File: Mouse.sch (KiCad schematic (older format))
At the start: 27 parts, among them J1 Conn_01x05_Male, U1 Left click, U2 Middle click, U3 Right Click, U4 LQ1, U5 Optical_Sensor

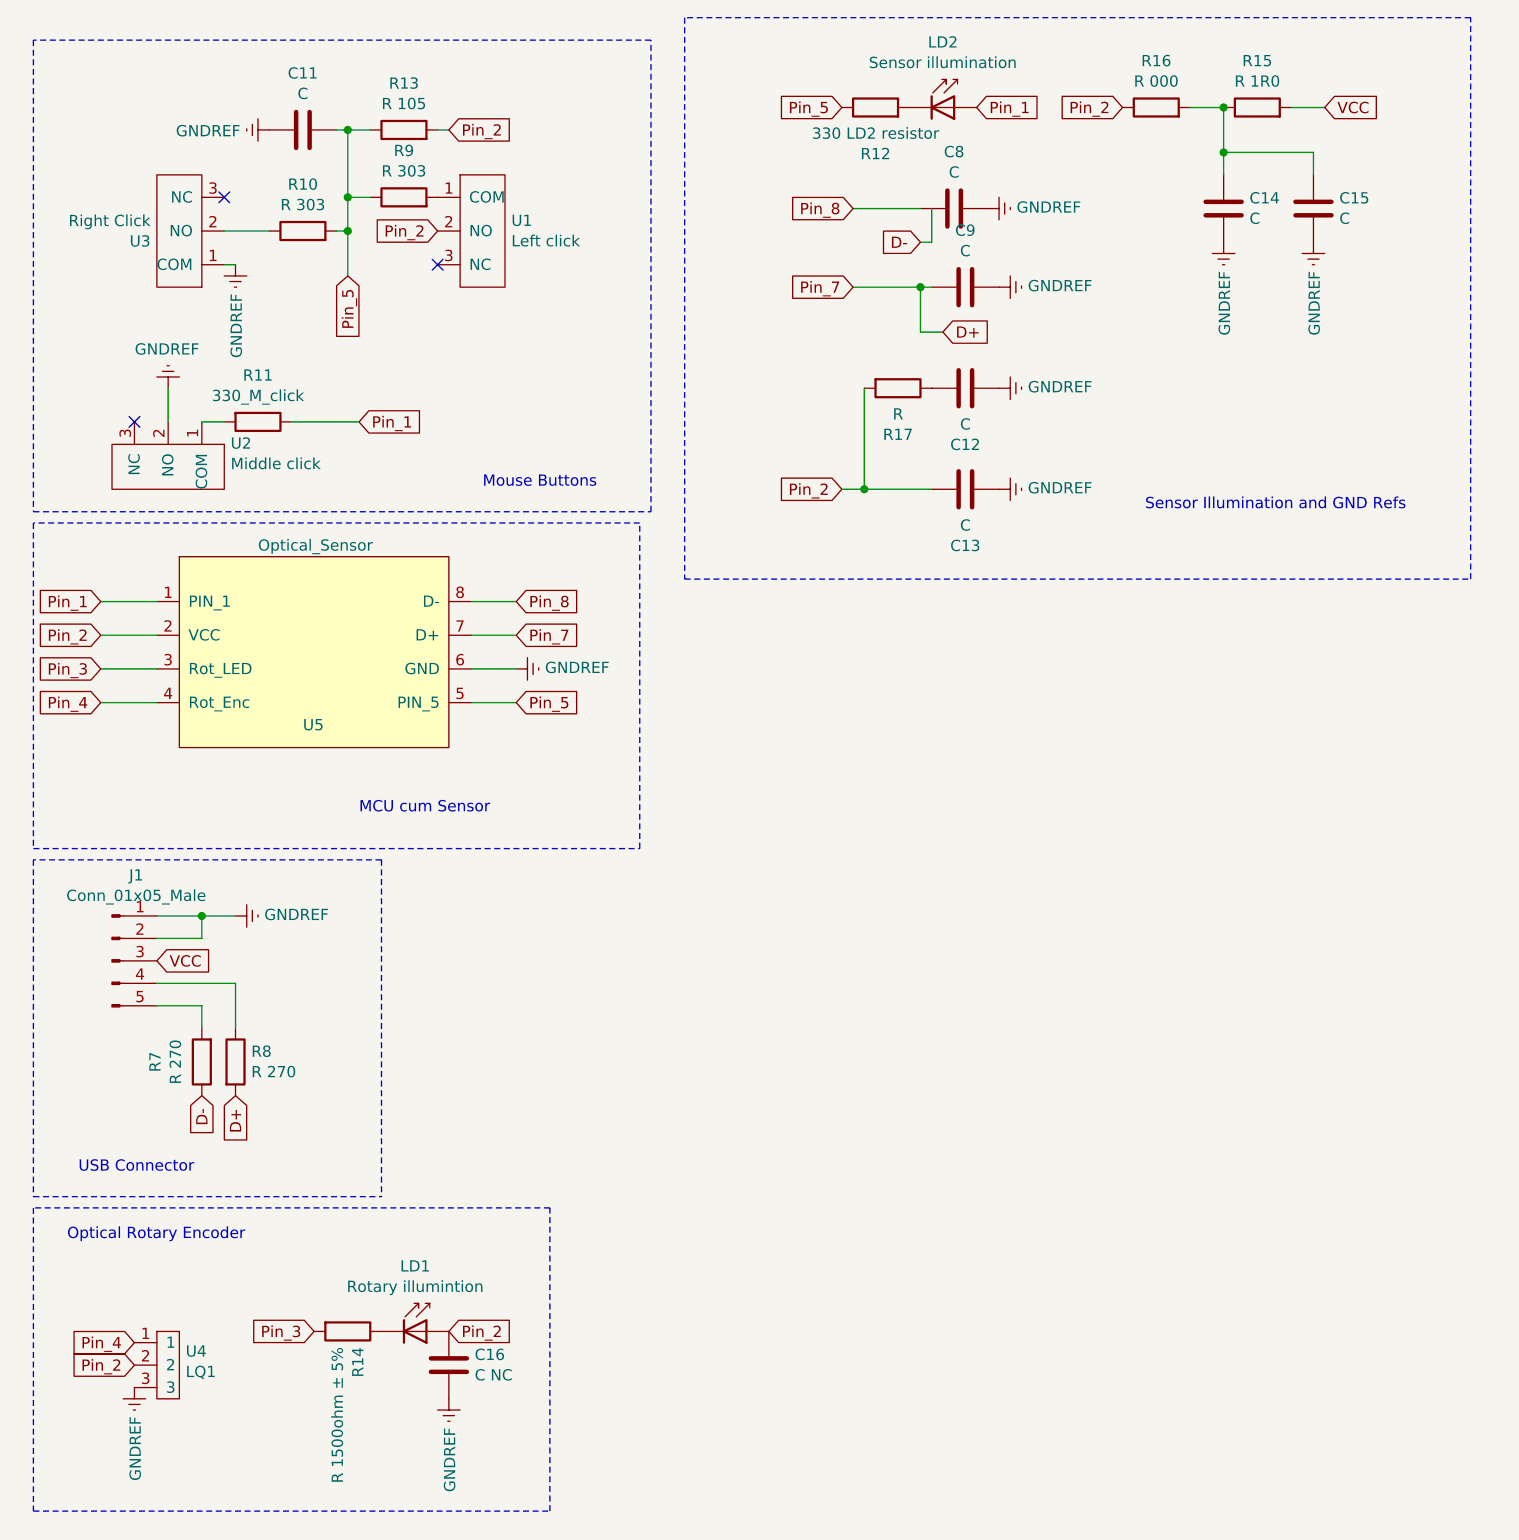
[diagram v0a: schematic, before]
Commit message: Updated layout
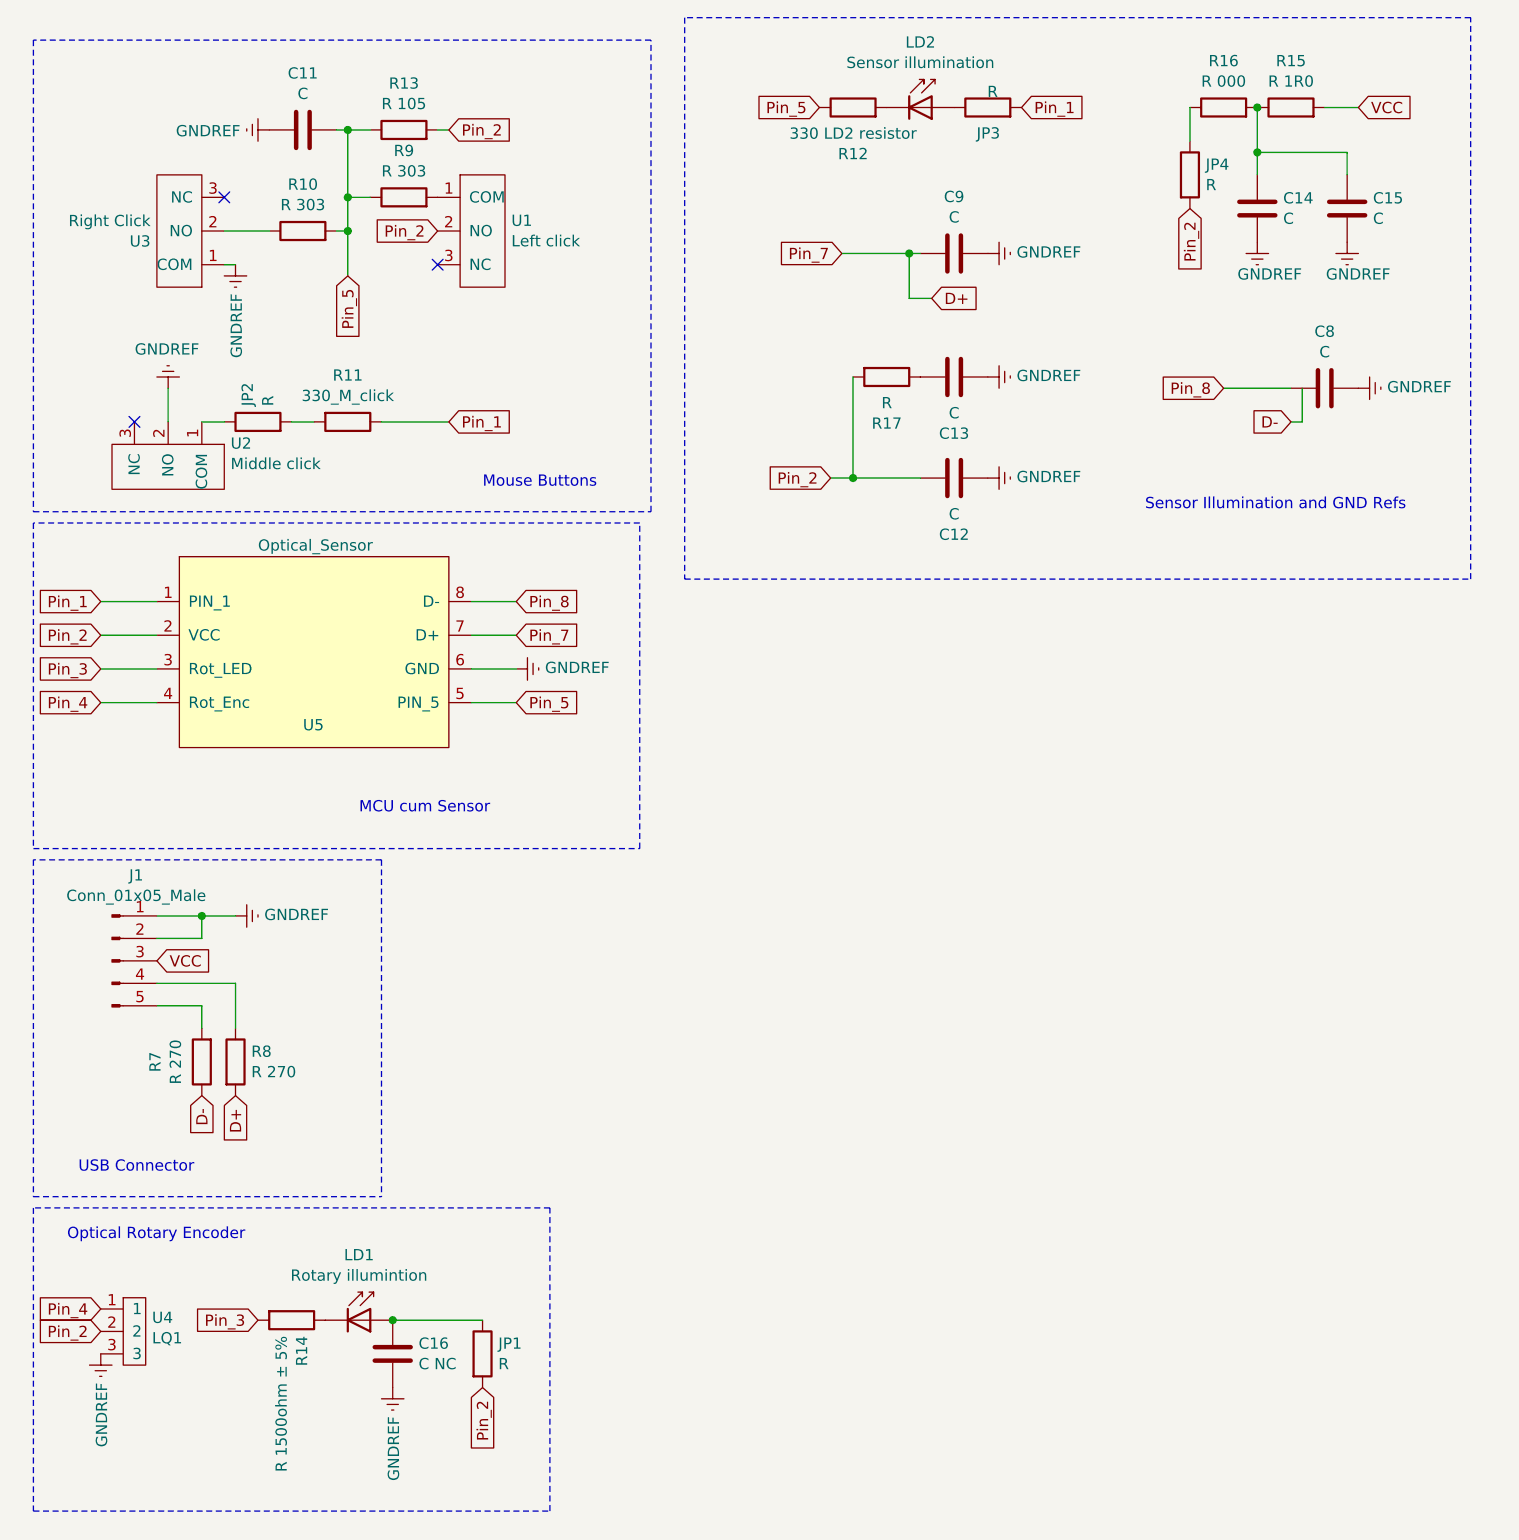
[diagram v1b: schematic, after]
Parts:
- added JP1, JP2, JP3, JP4: R, Resistor_THT:R_Axial_DIN0207_L6.3mm_D2.5mm_P10.16mm_Horizontal, symbol Device:R
- R14: footprint Resistor_SMD:R_0402_1005Metric_Pad0.72x0.64mm_HandSolder -> Resistor_THT:R_Axial_DIN0207_L6.3mm_D2.5mm_P10.16mm_Horizontal
- renumbered C13 to C12, C12 to C13
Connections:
- net Pin_1: now also JP3.2; no longer LD2.2 (A)
- net Pin_2: now also JP1.2, JP4.2; no longer C16.1, LD1.2 (A), R16.1
- net at U2.1 (COM): now also JP2.1; no longer R11.2
- new net: JP3.1, LD2.2 (A)
- new net: C16.1, JP1.1, LD1.2 (A)
- new net: JP2.2, R11.2
- new net: JP4.1, R16.1
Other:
- moved on the sheet: C12, C13, C14, C15, C16, C8, C9, LD1, LD2, R11, R12, R14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

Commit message: Updated board layout
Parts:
- C11, C12, C13, C8, C9: footprint Capacitor_SMD:C_0402_1005Metric_Pad0.74x0.62mm_HandSolder -> Mouse:R_0603_1608_Logi
- C14: footprint Capacitor_SMD:C_0201_0603Metric_Pad0.64x0.40mm_HandSolder -> Mouse:R_0603_1608_Logi
- C15, C16: footprint Capacitor_SMD:C_01005_0402Metric_Pad0.57x0.30mm_HandSolder -> Mouse:R_0603_1608_Logi
- JP1, JP2, JP3, JP4, R14: footprint Resistor_THT:R_Axial_DIN0207_L6.3mm_D2.5mm_P10.16mm_Horizontal -> Mouse:JP_Axial_DIN0207_L6.3mm_D2.5mm_P10.16mm_Horizontal
- LD1: footprint LED_THT:LED_D2.0mm_W4.0mm_H2.8mm_FlatTop -> Mouse:Rot_LED
- LD2: footprint LED_THT:LED_D5.0mm_Horizontal_O6.35mm_Z15.0mm -> Mouse:LED_Sensor
- R10, R11, R12, R13, R15, R16, R17, R7, R8, R9: footprint Resistor_SMD:R_01005_0402Metric_Pad0.57x0.30mm_HandSolder -> Mouse:R_0603_1608_Logi
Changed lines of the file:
@@
 F 0 "R17" V 4557 2200 50  0000 C CNN
 F 1 "R" V 4466 2200 50  0000 C CNN
-F 2 "Resistor_SMD:R_01005_0402Metric_Pad0.57x0.30mm_HandSolder" V 4280 2200 50  0001 C CNN
+F 2 "Mouse:R_0603_1608_Logi" V 4280 2200 50  0001 C CNN
 F 3 "~" H 4350 2200 50  0001 C CNN
 	1    4350 2200
@@
 F 0 "C13" V 4902 2200 50  0000 C CNN
 F 1 "C" V 4811 2200 50  0000 C CNN
-F 2 "Capacitor_SMD:C_0402_1005Metric_Pad0.74x0.62mm_HandSolder" H 4688 2050 50  0001 C CNN
+F 2 "Mouse:R_0603_1608_Logi" H 4688 2050 50  0001 C CNN
 F 3 "~" H 4650 2200 50  0001 C CNN
 	1    4650 2200
@@
 F 0 "R15" V 6357 1000 50  0000 C CNN
 F 1 "R 1R0" V 6266 1000 50  0000 C CNN
-F 2 "Resistor_SMD:R_01005_0402Metric_Pad0.57x0.30mm_HandSolder" V 6080 1000 50  0001 C CNN
+F 2 "Mouse:R_0603_1608_Logi" V 6080 1000 50  0001 C CNN
 F 3 "~" H 6150 1000 50  0001 C CNN
 	1    6150 1000
@@
 F 0 "R13" V 2407 1100 50  0000 C CNN
 F 1 "R 105" V 2316 1100 50  0000 C CNN
-F 2 "Resistor_SMD:R_01005_0402Metric_Pad0.57x0.30mm_HandSolder" V 2130 1100 50  0001 C CNN
+F 2 "Mouse:R_0603_1608_Logi" V 2130 1100 50  0001 C CNN
 F 3 "~" H 2200 1100 50  0001 C CNN
 	1    2200 1100
@@
 F 0 "C14" H 5885 1404 50  0000 R CNN
 F 1 "C" H 5885 1495 50  0000 R CNN
-F 2 "Capacitor_SMD:C_0201_0603Metric_Pad0.64x0.40mm_HandSolder" H 6038 1300 50  0001 C CNN
+F 2 "Mouse:R_0603_1608_Logi" H 6038 1300 50  0001 C CNN
 F 3 "~" H 6000 1450 50  0001 C CNN
 	1    6000 1450
@@
 F 0 "C15" H 6515 1496 50  0000 L CNN
 F 1 "C" H 6515 1405 50  0000 L CNN
-F 2 "Capacitor_SMD:C_01005_0402Metric_Pad0.57x0.30mm_HandSolder" H 6438 1300 50  0001 C CNN
+F 2 "Mouse:R_0603_1608_Logi" H 6438 1300 50  0001 C CNN
 F 3 "~" H 6400 1450 50  0001 C CNN
 	1    6400 1450
@@
 F 0 "C11" V 2002 1100 50  0000 C CNN
 F 1 "C" V 1911 1100 50  0000 C CNN
-F 2 "Capacitor_SMD:C_0402_1005Metric_Pad0.74x0.62mm_HandSolder" H 1788 950 50  0001 C CNN
+F 2 "Mouse:R_0603_1608_Logi" H 1788 950 50  0001 C CNN
 F 3 "~" H 1750 1100 50  0001 C CNN
 	1    1750 1100
@@
 F 0 "R9" V 2407 1400 50  0000 C CNN
 F 1 "R 303" V 2316 1400 50  0000 C CNN
-F 2 "Resistor_SMD:R_01005_0402Metric_Pad0.57x0.30mm_HandSolder" V 2130 1400 50  0001 C CNN
+F 2 "Mouse:R_0603_1608_Logi" V 2130 1400 50  0001 C CNN
 F 3 "~" H 2200 1400 50  0001 C CNN
 	1    2200 1400
@@
 F 0 "R10" V 1957 1550 50  0000 C CNN
 F 1 "R 303" V 1866 1550 50  0000 C CNN
-F 2 "Resistor_SMD:R_01005_0402Metric_Pad0.57x0.30mm_HandSolder" V 1680 1550 50  0001 C CNN
+F 2 "Mouse:R_0603_1608_Logi" V 1680 1550 50  0001 C CNN
 F 3 "~" H 1750 1550 50  0001 C CNN
 	1    1750 1550
@@
 F 0 "C9" V 4902 1650 50  0000 C CNN
 F 1 "C" V 4811 1650 50  0000 C CNN
-F 2 "Capacitor_SMD:C_0402_1005Metric_Pad0.74x0.62mm_HandSolder" H 4688 1500 50  0001 C CNN
+F 2 "Mouse:R_0603_1608_Logi" H 4688 1500 50  0001 C CNN
 F 3 "~" H 4650 1650 50  0001 C CNN
 	1    4650 1650
@@
 F 0 "C8" V 6552 2250 50  0000 C CNN
 F 1 "C" V 6461 2250 50  0000 C CNN
-F 2 "Capacitor_SMD:C_0402_1005Metric_Pad0.74x0.62mm_HandSolder" H 6338 2100 50  0001 C CNN
+F 2 "Mouse:R_0603_1608_Logi" H 6338 2100 50  0001 C CNN
 F 3 "~" H 6300 2250 50  0001 C CNN
 	1    6300 2250
@@
 F 0 "R7" V 1507 5250 50  0000 C CNN
 F 1 "R 270" V 1416 5250 50  0000 C CNN
-F 2 "Resistor_SMD:R_01005_0402Metric_Pad0.57x0.30mm_HandSolder" V 1230 5250 50  0001 C CNN
+F 2 "Mouse:R_0603_1608_Logi" V 1230 5250 50  0001 C CNN
 F 3 "~" H 1300 5250 50  0001 C CNN
 	1    1300 5250
@@
 F 0 "R8" H 1520 5296 50  0000 L CNN
 F 1 "R 270" H 1520 5205 50  0000 L CNN
-F 2 "Resistor_SMD:R_01005_0402Metric_Pad0.57x0.30mm_HandSolder" V 1380 5250 50  0001 C CNN
+F 2 "Mouse:R_0603_1608_Logi" V 1380 5250 50  0001 C CNN
 F 3 "~" H 1450 5250 50  0001 C CNN
 	1    1450 5250
@@
 F 0 "R11" V 1743 2400 50  0000 C CNN
 F 1 "330_M_click" V 1834 2400 50  0000 C CNN
-F 2 "Resistor_SMD:R_01005_0402Metric_Pad0.57x0.30mm_HandSolder" V 1880 2400 50  0001 C CNN
+F 2 "Mouse:R_0603_1608_Logi" V 1880 2400 50  0001 C CNN
 F 3 "~" H 1950 2400 50  0001 C CNN
 	1    1950 2400
@@
 F 0 "R14" H 1770 6446 50  0000 L CNN
 F 1 "R 1500ohm ± 5%" H 1770 6355 50  0000 L CNN
-F 2 "Resistor_THT:R_Axial_DIN0207_L6.3mm_D2.5mm_P10.16mm_Horizontal" V 1630 6400 50  0001 C CNN
+F 2 "Mouse:JP_Axial_DIN0207_L6.3mm_D2.5mm_P10.16mm_Horizontal" V 1630 6400 50  0001 C CNN
 F 3 "~" H 1700 6400 50  0001 C CNN
 	1    1700 6400
@@
 F 0 "C16" H 2265 6596 50  0000 L CNN
 F 1 "C NC" H 2265 6505 50  0000 L CNN
-F 2 "Capacitor_SMD:C_01005_0402Metric_Pad0.57x0.30mm_HandSolder" H 2188 6400 50  0001 C CNN
+F 2 "Mouse:R_0603_1608_Logi" H 2188 6400 50  0001 C CNN
 F 3 "~" H 2150 6550 50  0001 C CNN
 	1    2150 6550
@@
 F 0 "LD1" H 2000 6690 50  0000 C CNN
 F 1 "Rotary illumintion" H 2000 6599 50  0000 C CNN
-F 2 "LED_THT:LED_D2.0mm_W4.0mm_H2.8mm_FlatTop" H 2050 6575 50  0001 C CNN
+F 2 "Mouse:Rot_LED" H 2050 6575 50  0001 C CNN
 F 3 "http://www.alliedelec.com/m/d/40788c34903a719969df15f1fbea1056.pdf" H 2000 6400 50  0001 C CNN
 	1    2050 6400
@@
 F 0 "R12" V 3993 1000 50  0000 C CNN
 F 1 "330 LD2 resistor" V 4084 1000 50  0000 C CNN
-F 2 "Resistor_SMD:R_01005_0402Metric_Pad0.57x0.30mm_HandSolder" V 4130 1000 50  0001 C CNN
+F 2 "Mouse:R_0603_1608_Logi" V 4130 1000 50  0001 C CNN
 F 3 "~" H 4200 1000 50  0001 C CNN
 	1    4200 1000
@@
 F 0 "LD2" H 4500 1290 50  0000 C CNN
 F 1 "Sensor illumination" H 4500 1199 50  0000 C CNN
-F 2 "LED_THT:LED_D5.0mm_Horizontal_O6.35mm_Z15.0mm" H 4550 1175 50  0001 C CNN
+F 2 "Mouse:LED_Sensor" H 4550 1175 50  0001 C CNN
 F 3 "http://www.alliedelec.com/m/d/40788c34903a719969df15f1fbea1056.pdf" H 4500 1000 50  0001 C CNN
 	1    4550 1000
@@
 F 0 "C12" V 4902 2650 50  0000 C CNN
 F 1 "C" V 4811 2650 50  0000 C CNN
-F 2 "Capacitor_SMD:C_0402_1005Metric_Pad0.74x0.62mm_HandSolder" H 4688 2500 50  0001 C CNN
+F 2 "Mouse:R_0603_1608_Logi" H 4688 2500 50  0001 C CNN
 F 3 "~" H 4650 2650 50  0001 C CNN
 	1    4650 2650
@@
 F 0 "JP1" H 2620 6596 50  0000 L CNN
 F 1 "R" H 2620 6505 50  0000 L CNN
-F 2 "Resistor_THT:R_Axial_DIN0207_L6.3mm_D2.5mm_P10.16mm_Horizontal" V 2480 6550 50  0001 C CNN
+F 2 "Mouse:JP_Axial_DIN0207_L6.3mm_D2.5mm_P10.16mm_Horizontal" V 2480 6550 50  0001 C CNN
 F 3 "~" H 2550 6550 50  0001 C CNN
 	1    2550 6550
@@
 F 0 "JP2" H 1620 2446 50  0000 L CNN
 F 1 "R" H 1620 2355 50  0000 L CNN
-F 2 "Resistor_THT:R_Axial_DIN0207_L6.3mm_D2.5mm_P10.16mm_Horizontal" V 1480 2400 50  0001 C CNN
+F 2 "Mouse:JP_Axial_DIN0207_L6.3mm_D2.5mm_P10.16mm_Horizontal" V 1480 2400 50  0001 C CNN
 F 3 "~" H 1550 2400 50  0001 C CNN
 	1    1550 2400
@@
 F 0 "JP4" H 5770 1346 50  0000 L CNN
 F 1 "R" H 5770 1255 50  0000 L CNN
-F 2 "Resistor_THT:R_Axial_DIN0207_L6.3mm_D2.5mm_P10.16mm_Horizontal" V 5630 1300 50  0001 C CNN
+F 2 "Mouse:JP_Axial_DIN0207_L6.3mm_D2.5mm_P10.16mm_Horizontal" V 5630 1300 50  0001 C CNN
 F 3 "~" H 5700 1300 50  0001 C CNN
 	1    5700 1300
@@
 F 0 "JP3" V 4685 945 50  0000 L CNN
 F 1 "R" V 4870 955 50  0000 L CNN
-F 2 "Resistor_THT:R_Axial_DIN0207_L6.3mm_D2.5mm_P10.16mm_Horizontal" V 4730 1000 50  0001 C CNN
+F 2 "Mouse:JP_Axial_DIN0207_L6.3mm_D2.5mm_P10.16mm_Horizontal" V 4730 1000 50  0001 C CNN
 F 3 "~" H 4800 1000 50  0001 C CNN
 	1    4800 1000
@@
 F 0 "R16" V 6057 1000 50  0000 C CNN
 F 1 "R 000" V 5966 1000 50  0000 C CNN
-F 2 "Resistor_SMD:R_01005_0402Metric_Pad0.57x0.30mm_HandSolder" V 5780 1000 50  0001 C CNN
+F 2 "Mouse:R_0603_1608_Logi" V 5780 1000 50  0001 C CNN
 F 3 "~" H 5850 1000 50  0001 C CNN
 	1    5850 1000
